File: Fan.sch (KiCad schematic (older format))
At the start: 0 parts

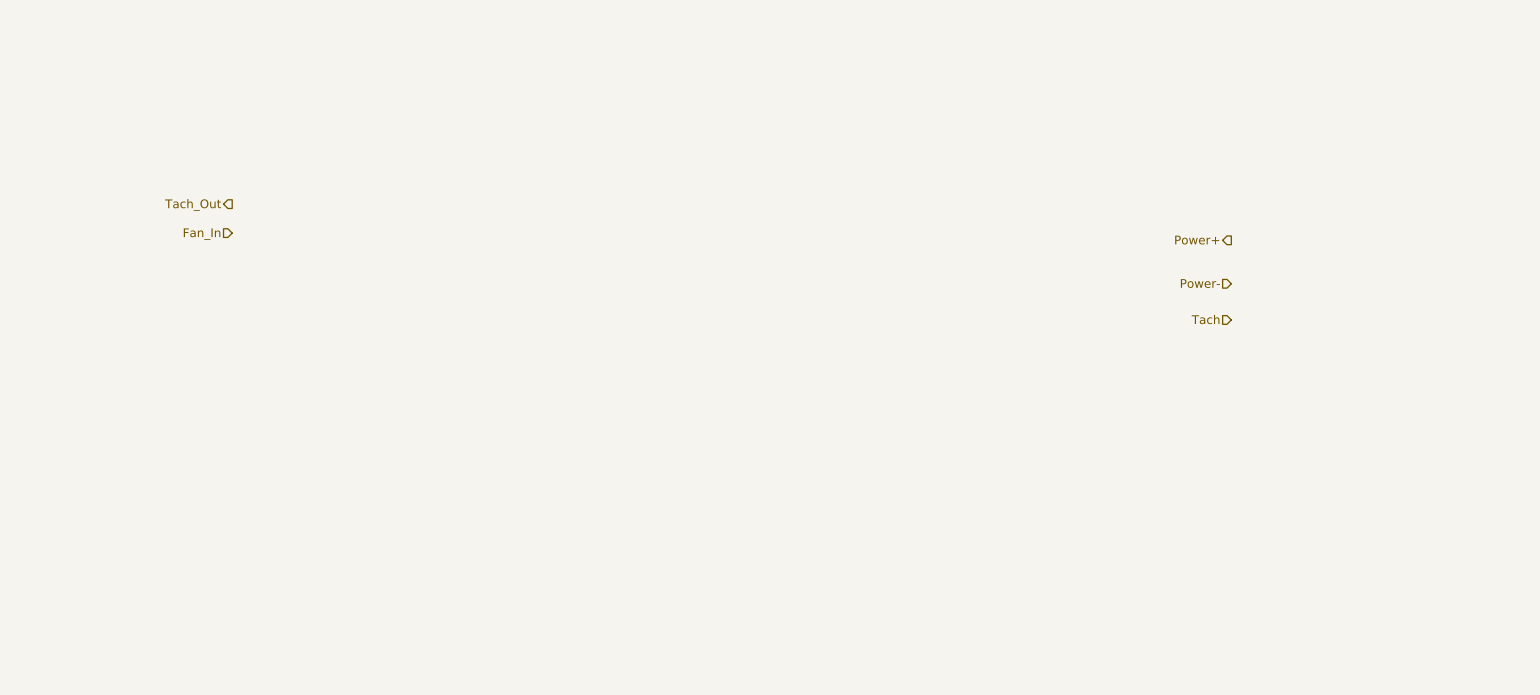
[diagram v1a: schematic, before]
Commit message: Create Initial Fan Module Schematic
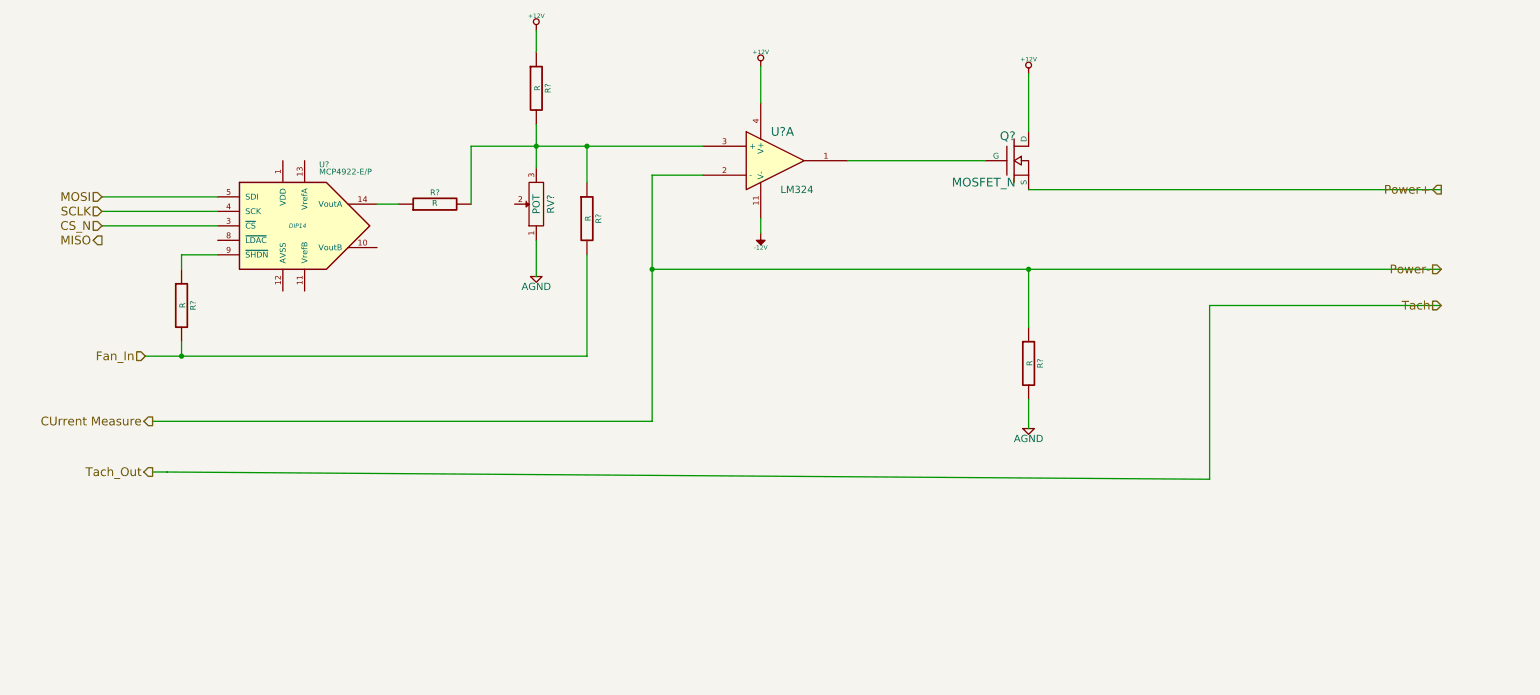
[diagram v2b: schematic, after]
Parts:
- added Q?: MOSFET_N, ~, symbol MOSFET_N
- added R? (x5): R, ~, symbol R
- added RV?: POT, ~, symbol POT
- added U?: LM324, symbol LM324
- added U?: MCP4922-E/P, DIP14, symbol MCP4922-E/P
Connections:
- net Fan_In: now also R?.2, R?.2
- net Power+: now also Q?.S
- new net: Q?.G, U?.1
- new net: R?.1, R?.2, R?.2, RV?.3, U?.3 (+)
- new net: R?.1, U?.14 (VoutA)
- new net: R?.1, U?.9 (~SHDN~)
- new net +12V: Q?.D, R?.1, U?.4 (V+)
- new net -12V: U?.11 (V-)
- new net AGND: R?.2, RV?.1
- new net CS_N: U?.3 (~CS~)
- new net CUrrent Measure: R?.1, U?.2 (-)
- new net MOSI: U?.5 (SDI)
- new net SCLK: U?.4 (SCK)

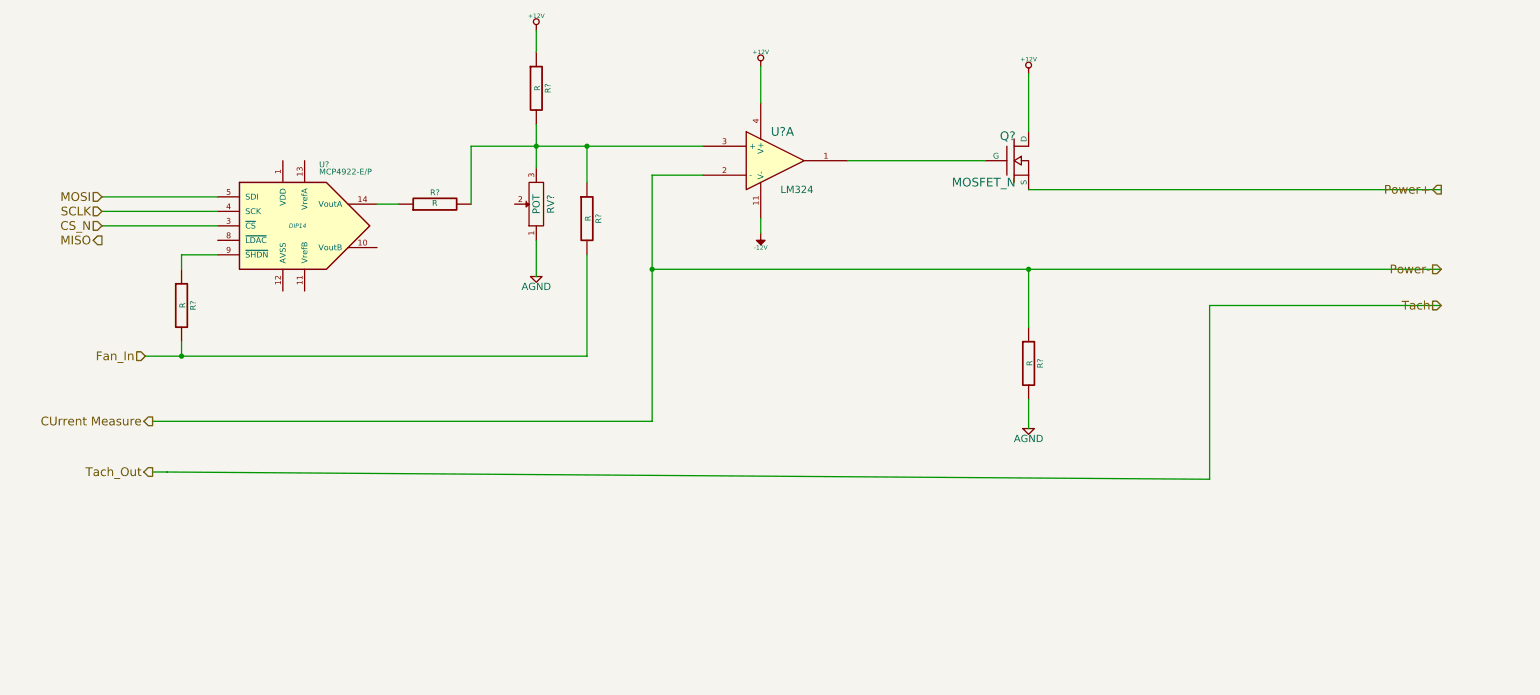
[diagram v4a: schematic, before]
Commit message: Create Arduino Schematic and Wire Up top Level
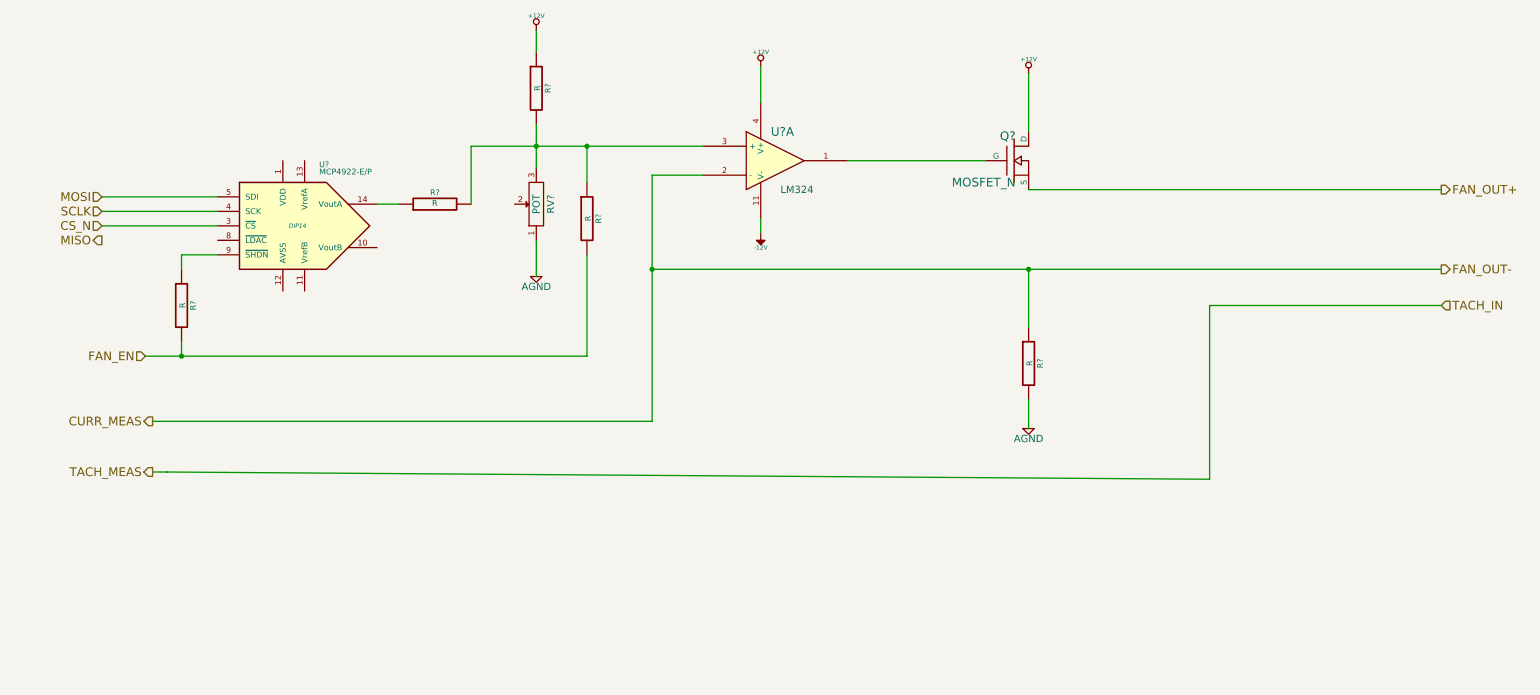
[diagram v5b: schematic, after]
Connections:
- net CUrrent Measure renamed CURR_MEAS
- net Fan_In renamed FAN_EN
- net Power+ renamed FAN_OUT+
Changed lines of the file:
@@
 Comment4 ""
 $EndDescr
-Text HLabel 10150 1900 0    60   Output ~ 0
-Power+
-Text HLabel 10150 2450 0    60   Input ~ 0
-Power-
-Text HLabel 10150 2700 0    60   Input ~ 0
-Tach
+Text HLabel 10150 1900 2    60   Output ~ 0
+FAN_OUT+
+Text HLabel 10150 2450 2    60   Output ~ 0
+FAN_OUT-
+Text HLabel 10150 2700 2    60   Input ~ 0
+TACH_IN
 Text HLabel 1250 3850 0    60   Output ~ 0
-Tach_Out
+TACH_MEAS
 Text HLabel 1200 3050 0    60   Input ~ 0
-Fan_In
+FAN_EN
 $Comp
 L LM324 U?
@@
 $EndComp
 Text HLabel 1250 3500 0    60   Output ~ 0
-CUrrent Measure
+CURR_MEAS
 Text HLabel 900  1950 0    60   Input ~ 0
 MOSI

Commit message: Upgrade Current/Fan Output Schem Use PWM
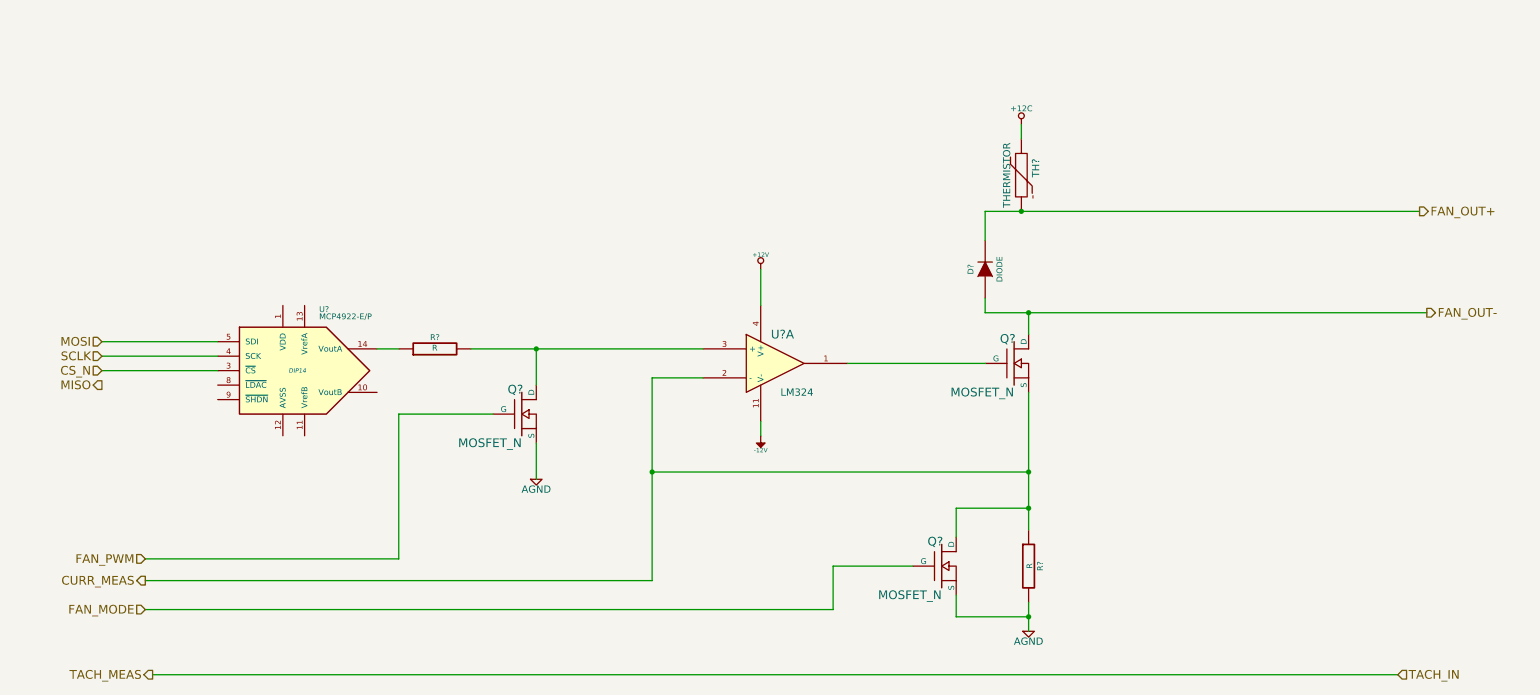
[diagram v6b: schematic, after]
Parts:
- removed R? (x3): R, ~, symbol R
- removed RV?: POT, ~, symbol POT
- added D?: DIODE, ~, symbol DIODE
- added Q? (x2): MOSFET_N, ~, symbol MOSFET_N
- added TH?: THERMISTOR, ~, symbol THERMISTOR
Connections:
- net +12V: no longer Q?.D
- net AGND: now also Q?.S, Q?.S
- net CURR_MEAS: now also Q?.S, Q?.D
- net FAN_OUT+: now also D?.2 (K), TH?.2; no longer Q?.S
- net at R?.2, U?.3 (+): now also Q?.D
- new net +12C: TH?.1
- new net FAN_MODE: Q?.G
- new net FAN_OUT-: D?.1 (A), Q?.D
- new net FAN_PWM: Q?.G
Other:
- moved on the sheet: Q?, R?, U?, U?A

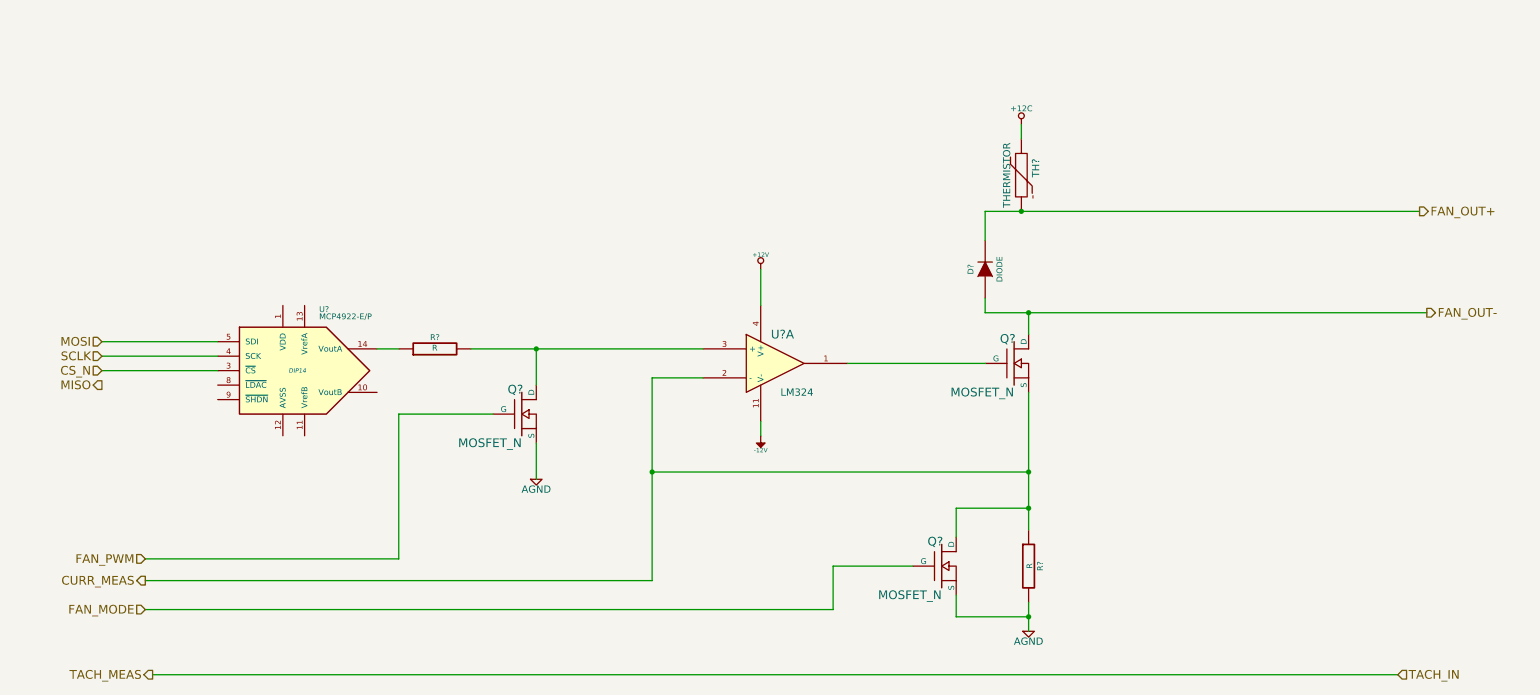
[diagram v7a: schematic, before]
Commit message: Added Arduino Connect Pin Layout
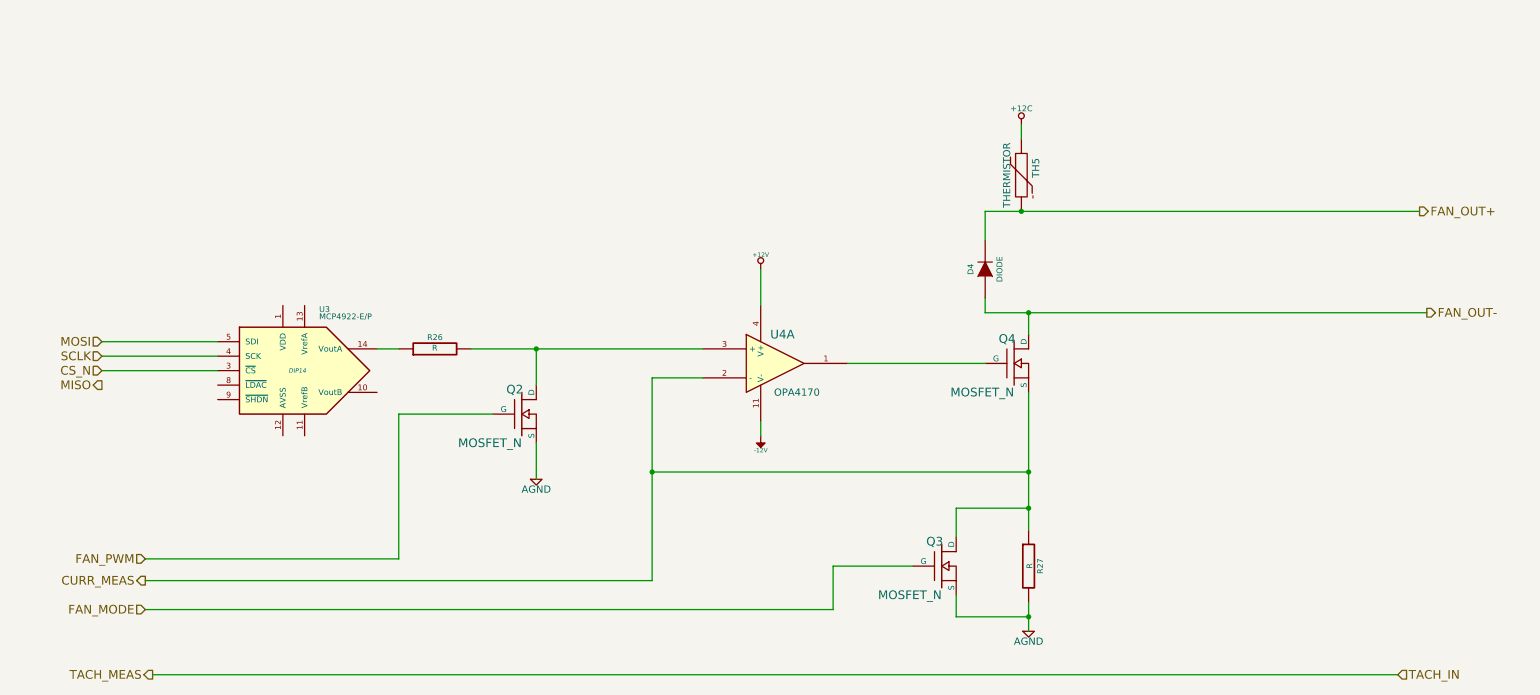
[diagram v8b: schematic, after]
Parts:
- U4: renamed from U?; value LM324 -> OPA4170
- gave numbers to parts that had none: 8
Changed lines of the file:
@@
 FAN_PWM
 $Comp
-L LM324 U?
+L LM324 U4
 U 1 1 52F18547
 P 5550 3100
-F 0 "U?" H 5600 3300 60  0000 C CNN
-F 1 "LM324" H 5700 2900 50  0000 C CNN
+F 0 "U4" H 5600 3300 60  0000 C CNN
+F 1 "OPA4170" H 5700 2900 50  0000 C CNN
 F 2 "" H 5550 3100 60  0000 C CNN
 F 3 "" H 5550 3100 60  0000 C CNN
@@
 $EndComp
 $Comp
-L MOSFET_N Q?
+L MOSFET_N Q4
 U 1 1 52F18565
 P 7200 3100
-F 0 "Q?" H 7210 3270 60  0000 R CNN
+F 0 "Q4" H 7210 3270 60  0000 R CNN
 F 1 "MOSFET_N" H 7200 2900 60  0000 R CNN
 F 2 "~" H 7200 3100 60  0000 C CNN
@@
 $EndComp
 $Comp
-L R R?
+L R R27
 U 1 1 52F1858E
 P 7300 4500
-F 0 "R?" V 7380 4500 40  0000 C CNN
+F 0 "R27" V 7380 4500 40  0000 C CNN
 F 1 "R" V 7307 4501 40  0000 C CNN
 F 2 "~" V 7230 4500 30  0000 C CNN
@@
 $EndComp
 $Comp
-L AGND #PWR?
+L AGND #PWR24
 U 1 1 52F185A4
 P 7300 4950
-F 0 "#PWR?" H 7300 4950 40  0001 C CNN
+F 0 "#PWR24" H 7300 4950 40  0001 C CNN
 F 1 "AGND" H 7300 4880 50  0000 C CNN
 F 2 "" H 7300 4950 60  0000 C CNN
@@
 $EndComp
 $Comp
-L -12V #PWR?
+L -12V #PWR22
 U 1 1 52F185C8
 P 5450 3600
-F 0 "#PWR?" H 5450 3730 20  0001 C CNN
+F 0 "#PWR22" H 5450 3730 20  0001 C CNN
 F 1 "-12V" H 5450 3700 30  0000 C CNN
 F 2 "" H 5450 3600 60  0000 C CNN
@@
 $EndComp
 $Comp
-L AGND #PWR?
+L AGND #PWR20
 U 1 1 52F18671
 P 3900 3900
-F 0 "#PWR?" H 3900 3900 40  0001 C CNN
+F 0 "#PWR20" H 3900 3900 40  0001 C CNN
 F 1 "AGND" H 3900 3830 50  0000 C CNN
 F 2 "" H 3900 3900 60  0000 C CNN
@@
 $EndComp
 $Comp
-L +12V #PWR?
+L +12V #PWR21
 U 1 1 52F18685
 P 5450 2450
-F 0 "#PWR?" H 5450 2400 20  0001 C CNN
+F 0 "#PWR21" H 5450 2400 20  0001 C CNN
 F 1 "+12V" H 5450 2550 30  0000 C CNN
 F 2 "" H 5450 2450 60  0000 C CNN
@@
 $EndComp
 $Comp
-L MCP4922-E/P U?
+L MCP4922-E/P U3
 U 1 1 52F19D27
 P 2250 3150
-F 0 "U?" H 2400 3550 40  0000 L BNN
+F 0 "U3" H 2400 3550 40  0000 L BNN
 F 1 "MCP4922-E/P" H 2400 3500 40  0000 L BNN
 F 2 "DIP14" H 2250 3150 30  0000 C CIN
@@
 SCLK
 $Comp
-L R R?
+L R R26
 U 1 1 52F19FD2
 P 3200 3000
-F 0 "R?" V 3280 3000 40  0000 C CNN
+F 0 "R26" V 3280 3000 40  0000 C CNN
 F 1 "R" V 3207 3001 40  0000 C CNN
 F 2 "~" V 3130 3000 30  0000 C CNN
@@
 	2800 3000 2950 3000
 $Comp
-L THERMISTOR TH?
+L THERMISTOR TH5
 U 1 1 52F79531
 P 7250 1800
-F 0 "TH?" V 7350 1850 50  0000 C CNN
+F 0 "TH5" V 7350 1850 50  0000 C CNN
 F 1 "THERMISTOR" V 7150 1800 50  0000 C CNN
 F 2 "~" H 7250 1800 60  0000 C CNN
@@
 	7000 2050 10000 2050
 $Comp
-L DIODE D?
+L DIODE D4
 U 1 1 52F7958D
 P 7000 2450
-F 0 "D?" H 7000 2550 40  0000 C CNN
+F 0 "D4" H 7000 2550 40  0000 C CNN
 F 1 "DIODE" H 7000 2350 40  0000 C CNN
 F 2 "~" H 7000 2450 60  0000 C CNN
@@
 Connection ~ 7250 2050
 $Comp
-L MOSFET_N Q?
+L MOSFET_N Q3
 U 1 1 52F795EF
 P 6700 4500
-F 0 "Q?" H 6710 4670 60  0000 R CNN
+F 0 "Q3" H 6710 4670 60  0000 R CNN
 F 1 "MOSFET_N" H 6700 4300 60  0000 R CNN
 F 2 "~" H 6700 4500 60  0000 C CNN
@@
 Connection ~ 7300 4850
 $Comp
-L MOSFET_N Q?
+L MOSFET_N Q2
 U 1 1 52F796D7
 P 3800 3450
-F 0 "Q?" H 3810 3620 60  0000 R CNN
+F 0 "Q2" H 3810 3620 60  0000 R CNN
 F 1 "MOSFET_N" H 3800 3250 60  0000 R CNN
 F 2 "~" H 3800 3450 60  0000 C CNN
@@
 	5950 4500 6500 4500
 $Comp
-L +12C #PWR?
+L +12C #PWR23
 U 1 1 52F79D10
 P 7250 1450
-F 0 "#PWR?" H 7250 1420 30  0001 C CNN
+F 0 "#PWR23" H 7250 1420 30  0001 C CNN
 F 1 "+12C" H 7250 1560 40  0000 C CNN
 F 2 "" H 7250 1450 60  0000 C CNN
